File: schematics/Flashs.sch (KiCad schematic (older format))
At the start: 23 parts

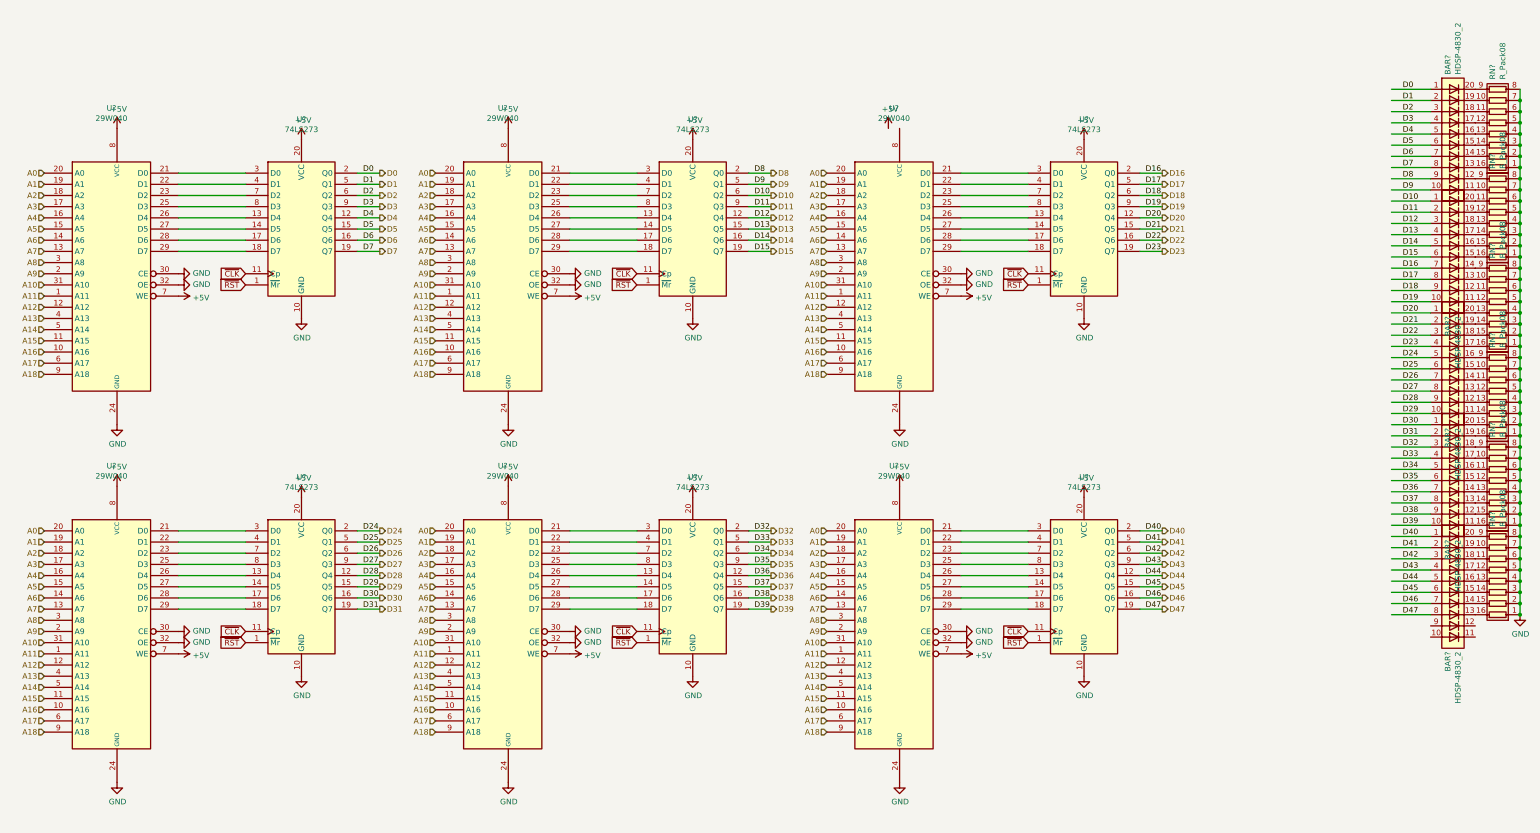
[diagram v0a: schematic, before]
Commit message: fix wrong microcode flashs
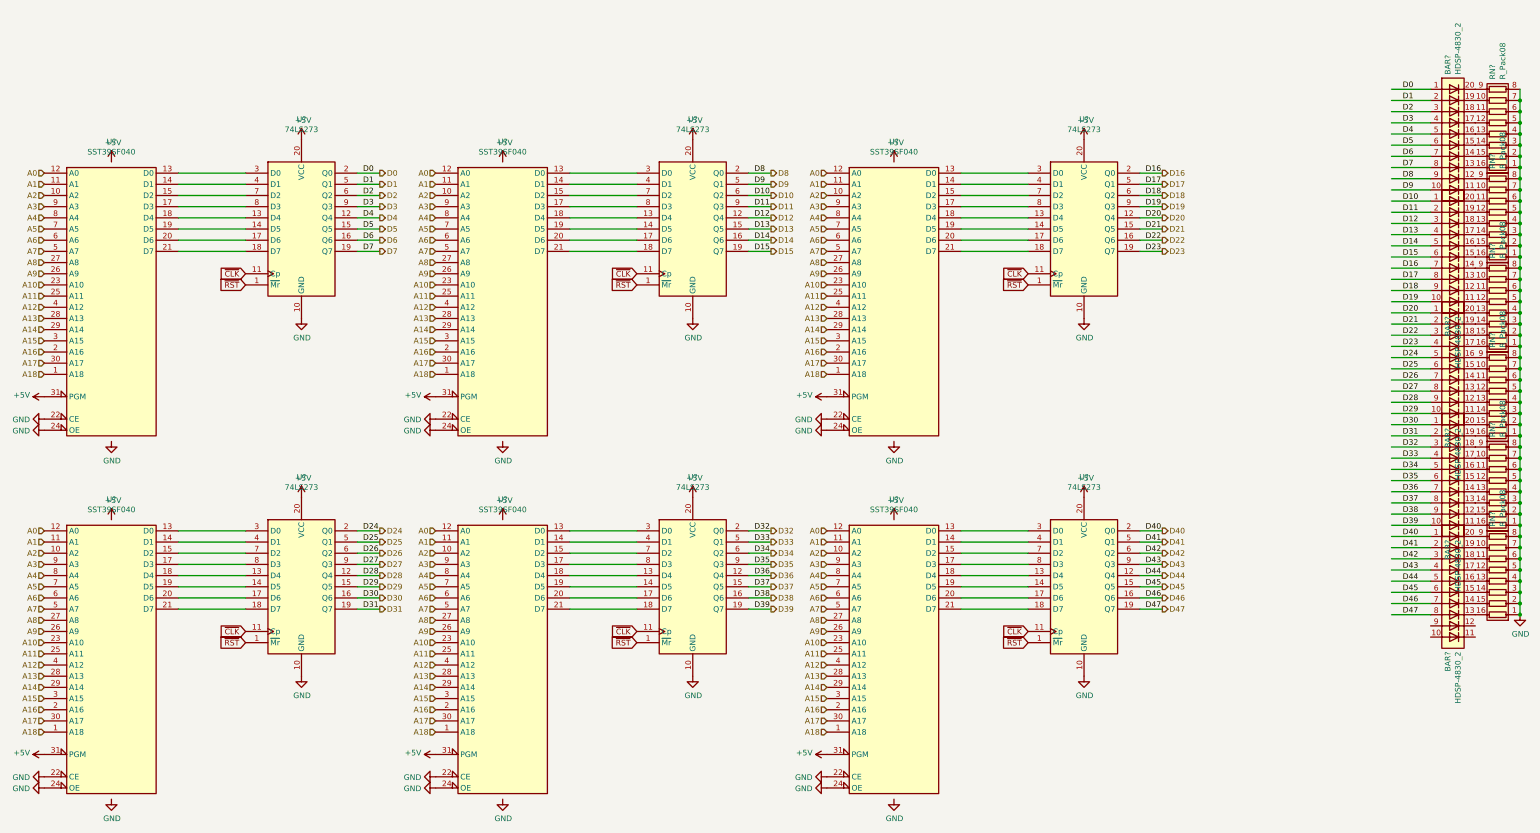
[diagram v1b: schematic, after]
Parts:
- removed U? (x6): 29W040, symbol Memory_Flash:29W040
- added U? (x6): SST39SF040, symbol Memory_Flash:SST39SF040
